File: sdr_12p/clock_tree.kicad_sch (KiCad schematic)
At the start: 83 parts, among them J34 Alt RF-In, J35 RPi, U15 HMC7043LP7FE, U21 ADF4351BCPZ, U4 ADF4351, U9 ADP150ACBZ-3.3-R7

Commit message: basic arrangement of blocks
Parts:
- removed U4: ADF4351, Package_CSP:LFCSP-32-1EP_5x5mm_P0.5mm_EP3.25x3.25mm, symbol Timer_PLL:ADF4351
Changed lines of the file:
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@@
-	)
-	(symbol
-		(lib_id "Timer_PLL:ADF4351")
-		(at 69.85 107.95 0)
-		(unit 1)
-		(exclude_from_sim no)
-		(in_bom yes)
-		(on_board yes)
-		(dnp no)
-		(fields_autoplaced yes)
-		(property "Reference" "U4"
-			(at 79.6133 77.47 0)
-			(effects
-				(font
-					(size 1.27 1.27)
-				)
-				(justify left)
-			)
-		)
-		(property "Value" "ADF4351"
-			(at 79.6133 80.01 0)
-			(effects
-				(font
-					(size 1.27 1.27)
-				)
-				(justify left)
-			)
-		)
-		(property "Footprint" "Package_CSP:LFCSP-32-1EP_5x5mm_P0.5mm_EP3.25x3.25mm"
-			(at 69.85 107.95 0)
-			(effects
-				(font
-					(size 1.27 1.27)
-				)
-				(hide yes)
-			)
-		)
-		(property "Datasheet" "https://www.analog.com/media/en/technical-documentation/data-sheets/ADF4351.pdf"
-			(at 69.85 107.95 0)
-			(effects
-				(font
-					(size 1.27 1.27)
-				)
-				(hide yes)
-			)
-		)
-		(property "Description" "35-4400MHz fractional-N PLL, LFCSP-32"
-			(at 69.85 107.95 0)
-			(effects
-				(font
-					(size 1.27 1.27)
-				)
-				(hide yes)
-			)
-		)
-		(pin "9"
-		)
-		(pin "26"
-		)
-		(pin "5"
-		)
-		(pin "3"
-		)
-		(pin "31"
-		)
-		(pin "4"
-		)
-		(pin "28"
-		)
-		(pin "11"
-		)
-		(pin "22"
-		)
-		(pin "6"
-		)
-		(pin "18"
-		)
-		(pin "30"
-		)
-		(pin "17"
-		)
-		(pin "20"
-		)
-		(pin "1"
-		)
-		(pin "19"
-		)
-		(pin "25"
-		)
-		(pin "7"
-		)
-		(pin "14"
-		)
-		(pin "21"
-		)
-		(pin "16"
-		)
-		(pin "32"
-		)
-		(pin "13"
-		)
-		(pin "33"
-		)
-		(pin "29"
-		)
-		(pin "2"
-		)
-		(pin "15"
-		)
-		(pin "24"
-		)
-		(pin "8"
-		)
-		(pin "12"
-		)
-		(pin "23"
-		)
-		(pin "10"
-		)
-		(pin "27"
-		)
-		(instances
-			(project ""
-				(path "/fe42ca2f-2bb8-4d5a-9e84-807788ed632f/79014999-6129-417a-b831-cb9e4a5873fe"
-					(reference "U4")
-					(unit 1)
-				)
-			)
-		)
 	)
 	(symbol

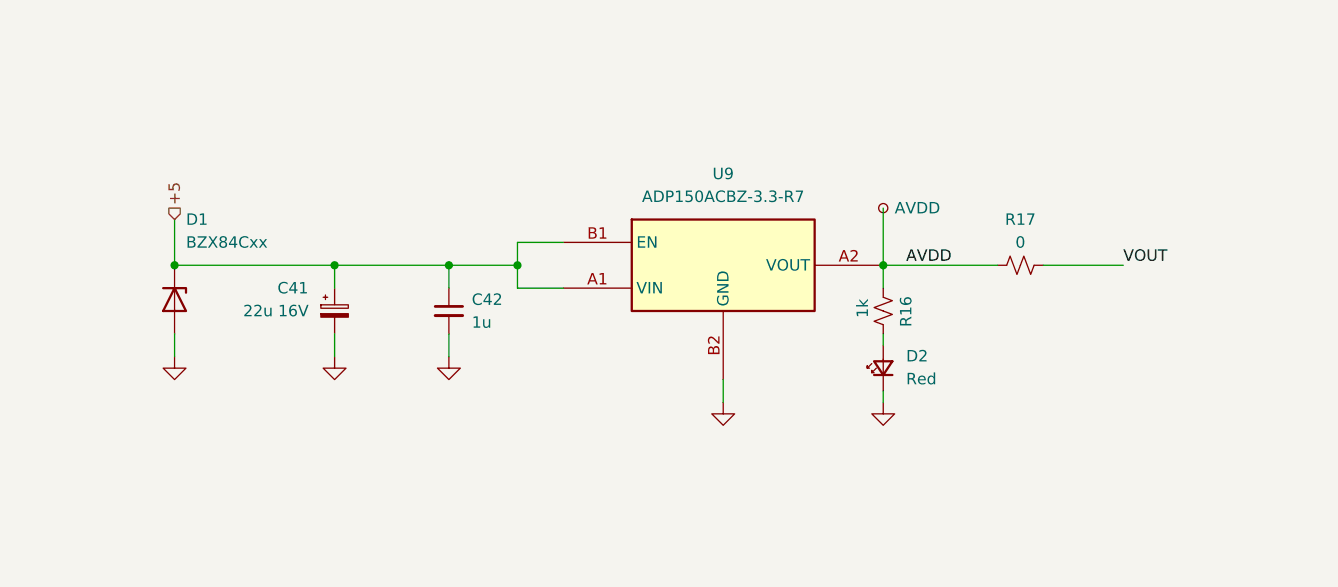
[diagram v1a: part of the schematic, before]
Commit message: fixed power ldo page
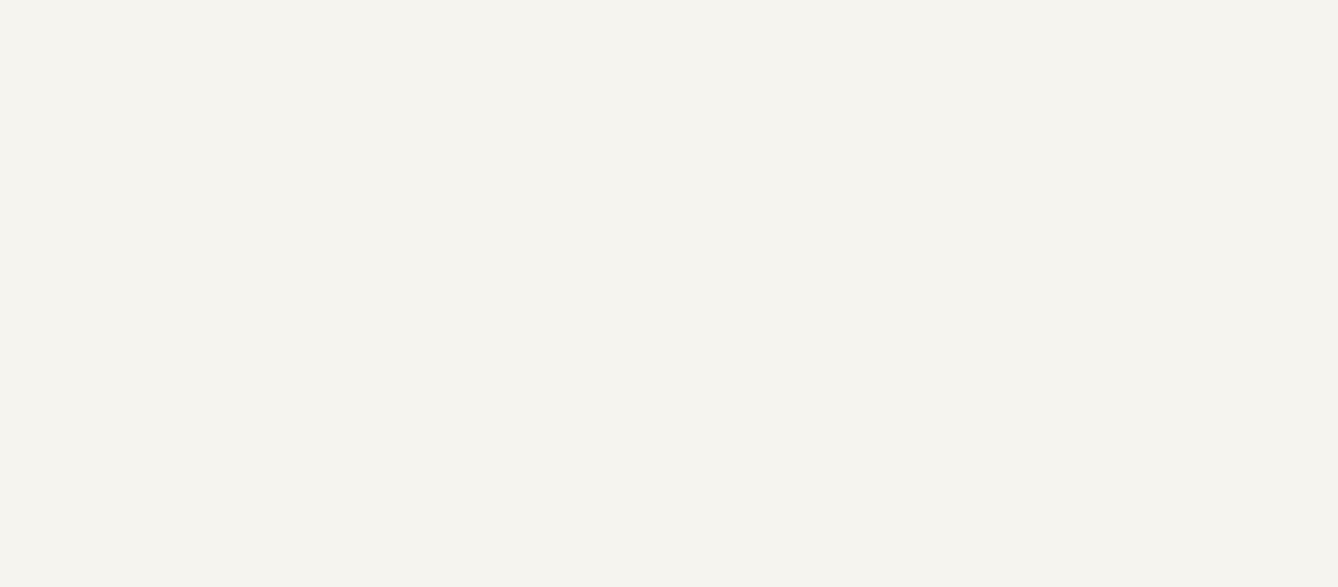
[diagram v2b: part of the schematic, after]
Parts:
- removed C41: 22u 16V, symbol Device:C_Polarized_Small
- removed C42: 1u, symbol Device:C_Small
- removed D1: BZX84Cxx, Package_TO_SOT_SMD:SOT-23, symbol Diode:BZX84Cxx
- removed D2: Red, symbol Device:LED_Small
- removed R16: 1k, symbol Device:R_Small_US
- removed R17: 0, symbol Device:R_Small_US
- removed TP1: AVDD, symbol Connector:TestPoint_Small
- removed U9: ADP150ACBZ-3.3-R7, hf-transceiver:CB_4_3_ADI, symbol hf-transceiver:ADP150ACBZ-3.3-R7

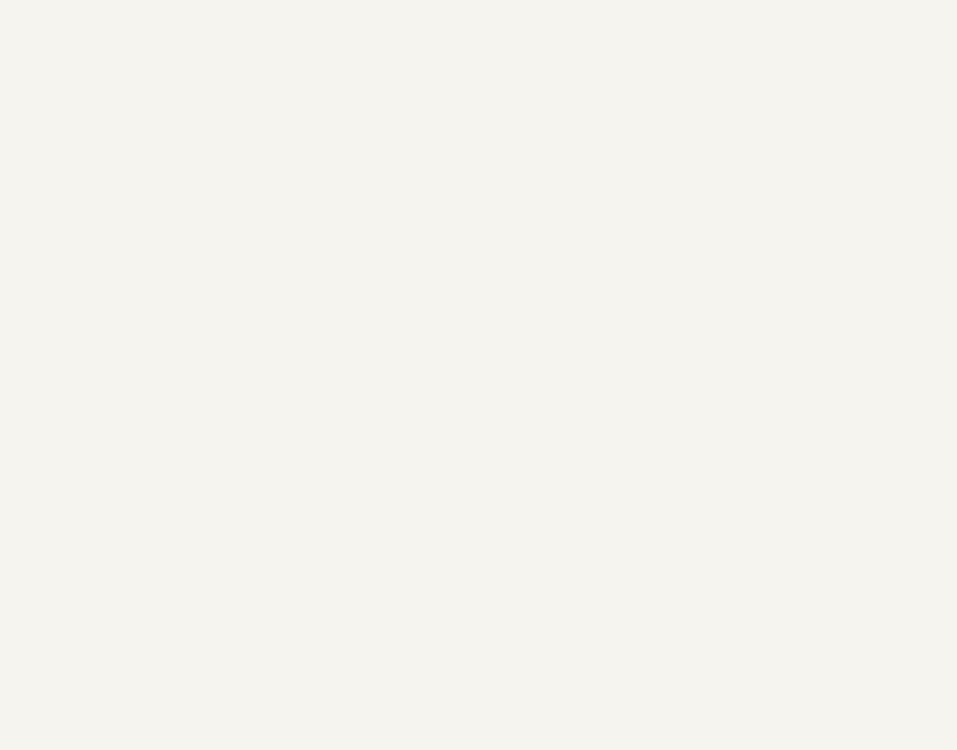
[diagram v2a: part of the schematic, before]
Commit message: fixed mixer page
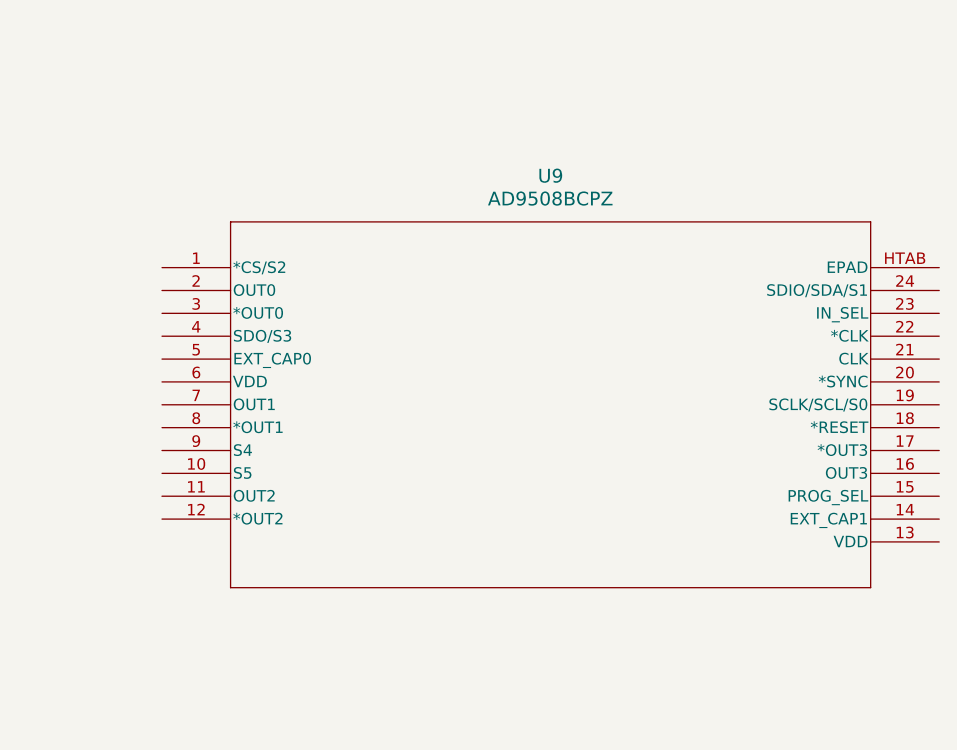
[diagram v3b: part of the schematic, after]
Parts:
- added U9: AD9508BCPZ, CP_24_7_ADI, symbol AD9508:AD9508BCPZ
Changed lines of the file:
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@@
+		)
+	)
+	(symbol
+		(lib_id "AD9508:AD9508BCPZ")
+		(at 260.35 52.07 0)
+		(unit 1)
+		(exclude_from_sim no)
+		(in_bom yes)
+		(on_board yes)
+		(dnp no)
+		(fields_autoplaced yes)
+		(property "Reference" "U9"
+			(at 303.53 41.91 0)
+			(effects
+				(font
+					(size 1.524 1.524)
+				)
+			)
+		)
+		(property "Value" "AD9508BCPZ"
+			(at 303.53 44.45 0)
+			(effects
+				(font
+					(size 1.524 1.524)
+				)
+			)
+		)
+		(property "Footprint" "CP_24_7_ADI"
+			(at 260.35 52.07 0)
+			(effects
+				(font
+					(size 1.27 1.27)
+					(italic yes)
+				)
+				(hide yes)
+			)
+		)
+		(property "Datasheet" "https://www.analog.com/media/en/technical-documentation/data-sheets/AD9508.pdf"
+			(at 260.35 52.07 0)
+			(effects
+				(font
+					(size 1.27 1.27)
+					(italic yes)
+				)
+				(hide yes)
+			)
+		)
+		(property "Description" ""
+			(at 260.35 52.07 0)
+			(effects
+				(font
+					(size 1.27 1.27)
+				)
+				(hide yes)
+			)
+		)
+		(pin "9"
+		)
+		(pin "17"
+		)
+		(pin "11"
+		)
+		(pin "7"
+		)
+		(pin "14"
+		)
+		(pin "8"
+		)
+		(pin "19"
+		)
+		(pin "23"
+		)
+		(pin "20"
+		)
+		(pin "24"
+		)
+		(pin "12"
+		)
+		(pin "1"
+		)
+		(pin "2"
+		)
+		(pin "15"
+		)
+		(pin "HTAB"
+		)
+		(pin "21"
+		)
+		(pin "16"
+		)
+		(pin "3"
+		)
+		(pin "6"
+		)
+		(pin "13"
+		)
+		(pin "10"
+		)
+		(pin "22"
+		)
+		(pin "18"
+		)
+		(pin "5"
+		)
+		(pin "4"
+		)
+		(instances
+			(project ""
+				(path "/fe42ca2f-2bb8-4d5a-9e84-807788ed632f/79014999-6129-417a-b831-cb9e4a5873fe"
+					(reference "U9")
+					(unit 1)
+				)
+			)
 		)
 	)

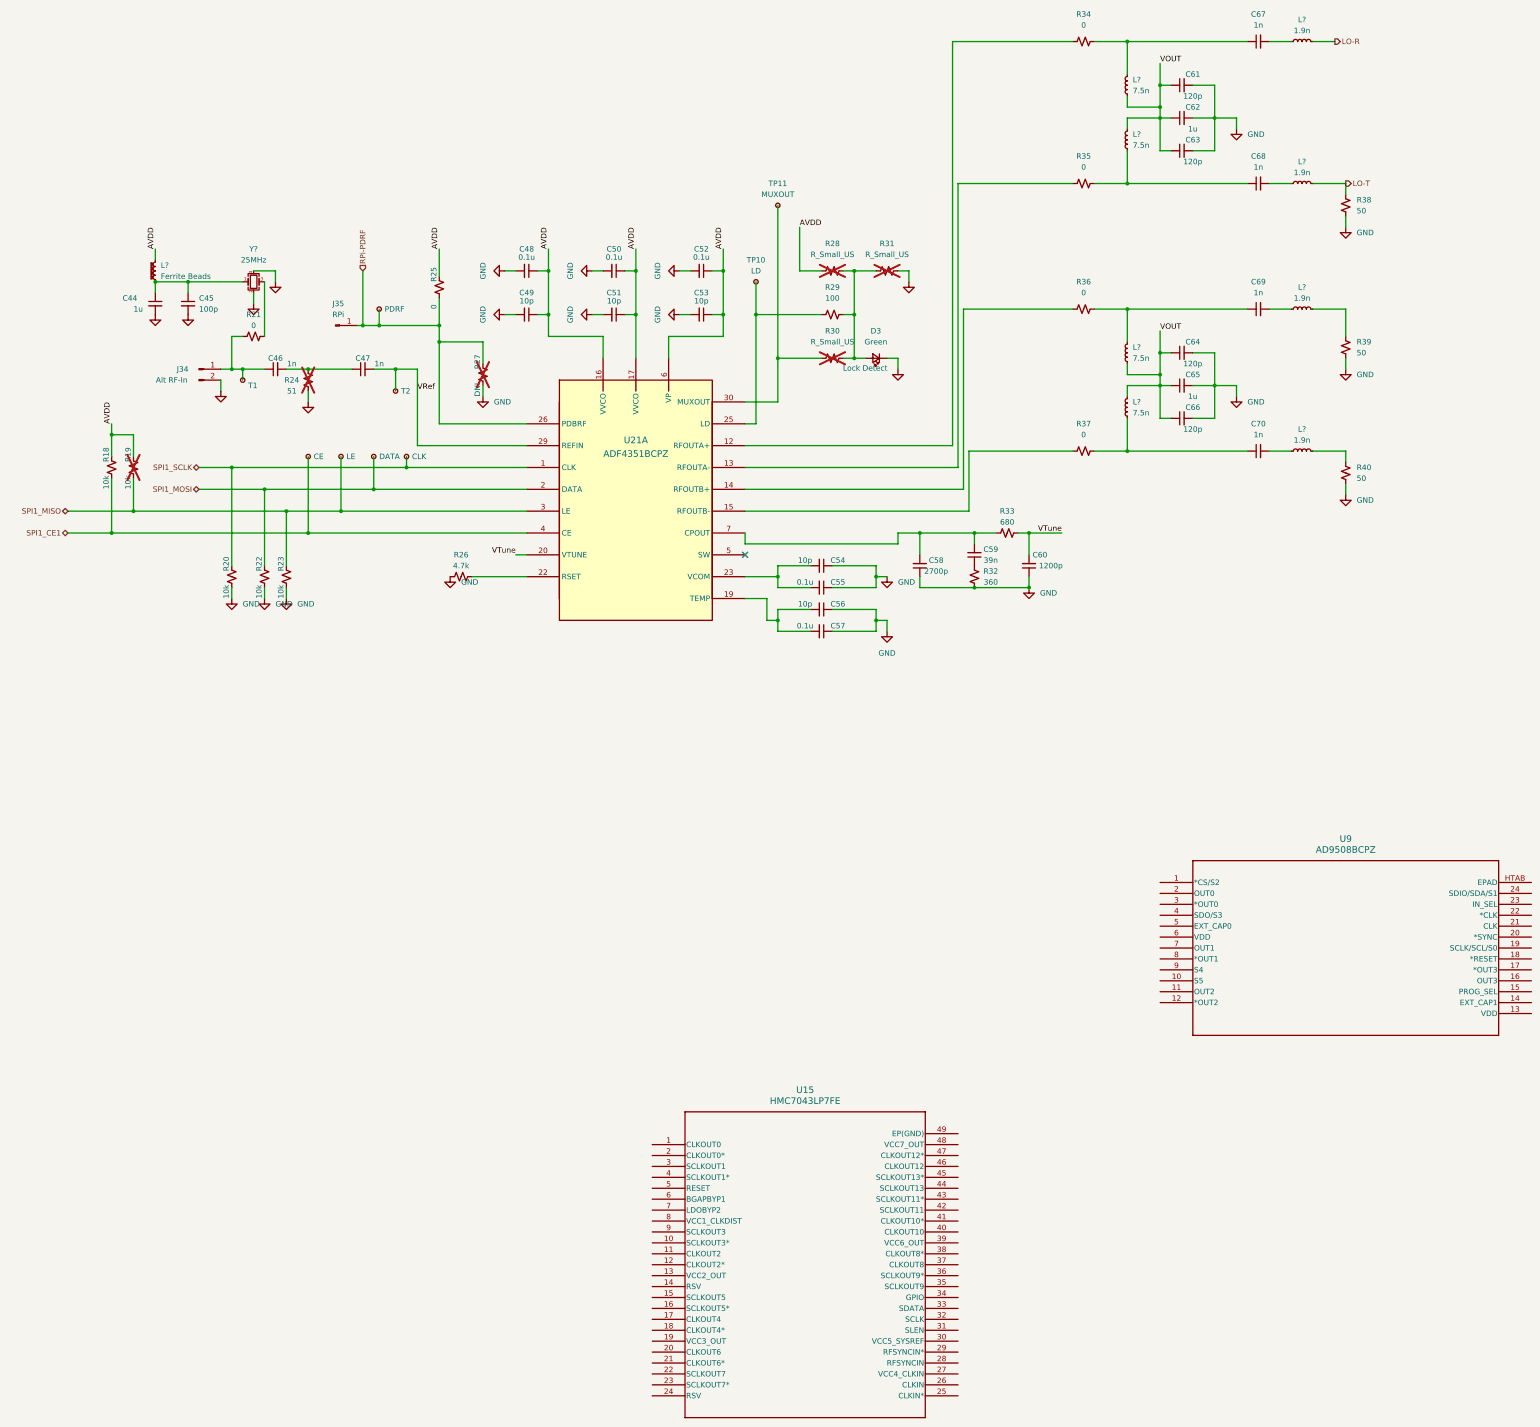
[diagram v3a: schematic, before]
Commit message: fixed ldos for Clocks and DAP
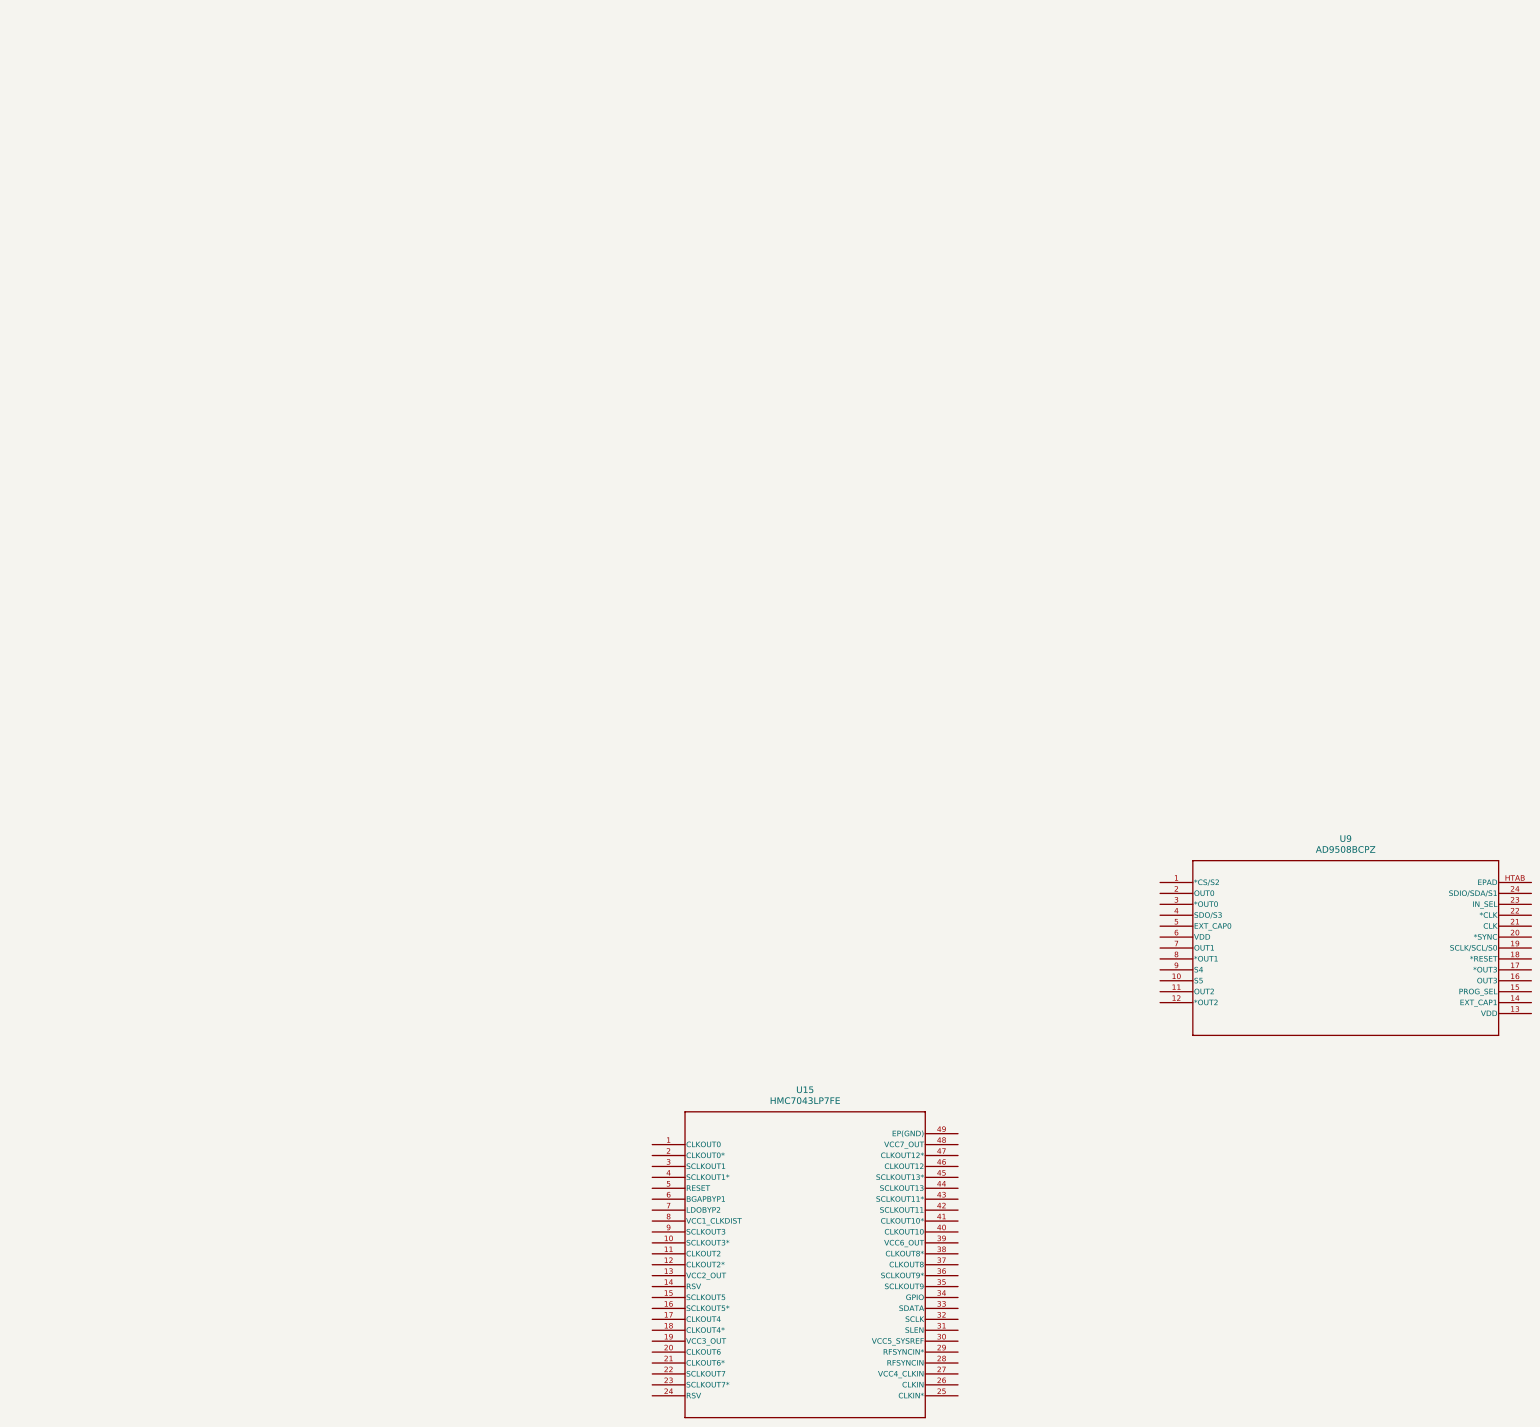
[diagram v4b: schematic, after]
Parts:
- removed C44, C62, C65: 1u, symbol Device:C_Small
- removed C45: 100p, symbol Device:C_Small
- removed C46, C47, C67, C68, C69, C70: 1n, symbol Device:C_Small
- removed C48, C50, C52, C55, C57: 0.1u, symbol Device:C_Small
- removed C49, C51, C53, C54, C56: 10p, symbol Device:C_Small
- removed C58: 2700p, symbol Device:C_Small
- removed C59: 39n, symbol Device:C_Small
- removed C60: 1200p, symbol Device:C_Small
- removed C61, C63, C64, C66: 120p, symbol Device:C_Small
- removed D3: Green, symbol Device:LED_Small
- removed J34: Alt RF-In, symbol Connector:Conn_01x02_Pin
- removed J35: RPi, symbol Connector:Conn_01x01_Pin
- removed L? (x4): 1.9n, symbol Device:L_Small
- removed L?: Ferrite Beads, symbol Device:L_Ferrite_Small
- removed L? (x4): 7.5n, symbol Device:L_Small
- removed R18, R19, R20, R22, R23: 10k, symbol Device:R_Small_US
- removed R21, R25, R34, R35, R36, R37: 0, symbol Device:R_Small_US
- removed R24: 51, symbol Device:R_Small_US
- removed R26: 4.7k, symbol Device:R_Small_US
- removed R27: DNI, symbol Device:R_Small_US
- removed R28, R30, R31: R_Small_US, symbol Device:R_Small_US
- removed R29: 100, symbol Device:R_Small_US
- removed R32: 360, symbol Device:R_Small_US
- removed R33: 680, symbol Device:R_Small_US
- removed R38, R39, R40: 50, symbol Device:R_Small_US
- removed TP10: LD, symbol Connector:TestPoint_Small
- removed TP11: MUXOUT, symbol Connector:TestPoint_Small
- removed TP3: T1, symbol Connector:TestPoint_Small
- removed TP4: CE, symbol Connector:TestPoint_Small
- removed TP5: LE, symbol Connector:TestPoint_Small
- removed TP6: DATA, symbol Connector:TestPoint_Small
- removed TP7: PDRF, symbol Connector:TestPoint_Small
- removed TP8: T2, symbol Connector:TestPoint_Small
- removed TP9: CLK, symbol Connector:TestPoint_Small
- removed U21: ADF4351BCPZ, hf-transceiver:CP-32-7_ADI, symbol hf-transceiver:ADF4351BCPZ
- removed Y?: 25MHz, symbol Device:Crystal_GND24_Small
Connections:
- no-connect marks 1 -> 0
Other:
- note removed: "Lock Detect"
